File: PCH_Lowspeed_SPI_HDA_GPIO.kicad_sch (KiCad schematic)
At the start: 1 part

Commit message: Some DP and power work
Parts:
- added R1, R3: 30Ω, Resistor_SMD:R_0402_1005Metric, symbol Device:R_Small
- added R2: 20Ω, Resistor_SMD:R_0402_1005Metric, symbol Device:R_Small
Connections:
- net iGPU_DDI1_SCL: now reaches UPCH1.AL13 (GPP_I5/DDPB_CTRLCLK)
- net iGPU_DDI1_SDA: now reaches UPCH1.AR8 (GPP_I6/DDPB_CTRLDATA)
- net at UPCH1.AM2 (HDACPU_SDO): now also R1.2
- net at UPCH1.AM3 (HDACPU_SCLK): now also R3.2
- net at UPCH1.AN3 (HDACPU_SDI): now also R2.2
- new net CPU_DisplayAudio_CLK: R3.1
- new net CPU_DisplayAudio_SDI: R1.1
- new net CPU_DisplayAudio_SDO: R2.1

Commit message: More DP
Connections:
- net iGPU_DDI2_SDA: now reaches UPCH1.AL10 (GPP_I8/DDPC_CTRLDATA)
- net iGPU_DDI3_SCL: now reaches UPCH1.AL9 (GPP_I9/DDPD_CTRLCLK)
- net iGPU_DDI2_SCL: now reaches UPCH1.AN13 (GPP_I7/DDPC_CTRLCLK)
- net iGPU_DDI3_SDA: now reaches UPCH1.AR3 (GPP_I10/DDPD_CTRLDATA)
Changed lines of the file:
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@@
+	(wire
+		(pts
+			(xy 120.65 123.19) (xy 115.57 123.19)
+		)
+		(stroke
+			(width 0)
+			(type default)
+		)
+	)
 	(wire
 		(pts
@@
 	(wire
 		(pts
+			(xy 120.65 130.81) (xy 115.57 130.81)
+		)
+		(stroke
+			(width 0)
+			(type default)
+		)
+	)
+	(wire
+		(pts
+			(xy 120.65 128.27) (xy 115.57 128.27)
+		)
+		(stroke
+			(width 0)
+			(type default)
+		)
+	)
+	(wire
+		(pts
+			(xy 120.65 125.73) (xy 115.57 125.73)
+		)
+		(stroke
+			(width 0)
+			(type default)
+		)
+	)
+	(wire
+		(pts
 			(xy 158.75 57.15) (xy 162.56 57.15)
 		)
@@
 		)
 	)
+	(global_label "iGPU_DDI3_SDA"
+		(shape input)
+		(at 120.65 130.81 0)
+		(fields_autoplaced yes)
+		(effects
+			(font
+				(size 1.27 1.27)
+			)
+			(justify left)
+		)
+		(property "Intersheetrefs" "${INTERSHEET_REFS}"
+			(at 144.9831 130.81 0)
+			(effects
+				(font
+					(size 1.27 1.27)
+				)
+				(justify left)
+				(hide yes)
+			)
+		)
+	)
+	(global_label "iGPU_DDI2_SCL"
+		(shape input)
+		(at 120.65 123.19 0)
+		(fields_autoplaced yes)
+		(effects
+			(font
+				(size 1.27 1.27)
+			)
+			(justify left)
+		)
+		(property "Intersheetrefs" "${INTERSHEET_REFS}"
+			(at 144.9831 123.19 0)
+			(effects
+				(font
+					(size 1.27 1.27)
+				)
+				(justify left)
+				(hide yes)
+			)
+		)
+	)
 	(global_label "CPU_DisplayAudio_CLK"
 		(shape input)
@@
 		)
 	)
+	(global_label "iGPU_DDI3_SCL"
+		(shape input)
+		(at 120.65 128.27 0)
+		(fields_autoplaced yes)
+		(effects
+			(font
+				(size 1.27 1.27)
+			)
+			(justify left)
+		)
+		(property "Intersheetrefs" "${INTERSHEET_REFS}"
+			(at 144.9831 128.27 0)
+			(effects
+				(font
+					(size 1.27 1.27)
+				)
+				(justify left)
+				(hide yes)
+			)
+		)
+	)
 	(global_label "iGPU_DDI1_SCL"
 		(shape input)
@@
 			(effects
 				(font
+					(size 1.27 1.27)
+				)
+				(justify left)
+				(hide yes)
+			)
+		)
+	)
+	(global_label "iGPU_DDI2_SDA"
+		(shape input)
+		(at 120.65 125.73 0)
+		(fields_autoplaced yes)
+		(effects
+			(font
+				(size 1.27 1.27)
+			)
+			(justify left)
+		)
+		(property "Intersheetrefs" "${INTERSHEET_REFS}"
+			(at 144.9831 125.73 0)
+			(effects
+				(font

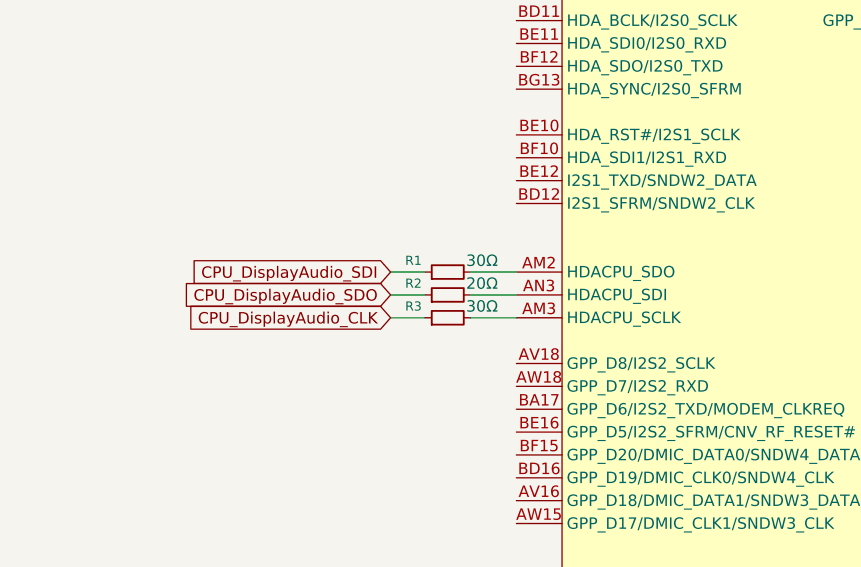
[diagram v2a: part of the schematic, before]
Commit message: Added PCH SKU IO table screenshot from datasheet to schematic
and a note about display audio
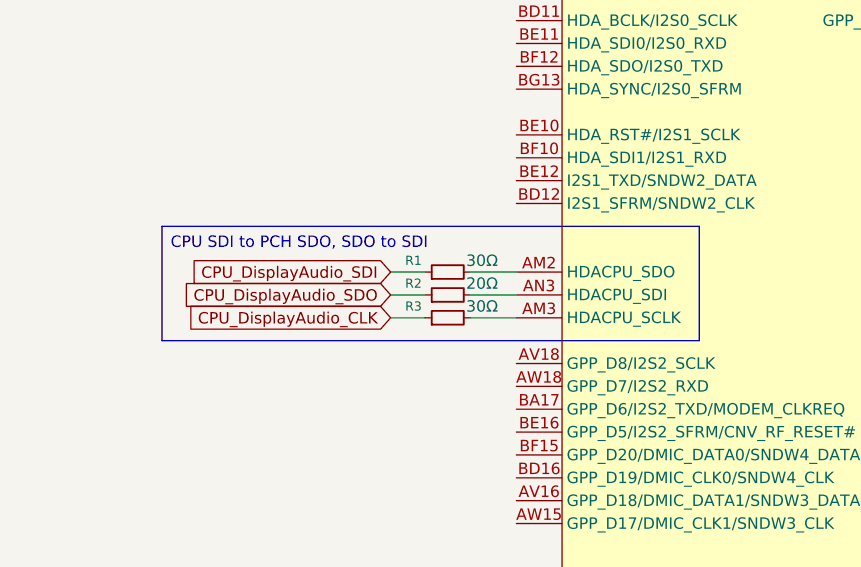
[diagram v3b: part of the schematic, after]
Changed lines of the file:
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@@
 		(company "WifiCable")
+	)
+	(text_box "CPU SDI to PCH SDO, SDO to SDI"
+		(exclude_from_sim no)
+		(at 133.35 52.07 0)
+		(size 59.69 12.7)
+		(margins 0.9525 0.9525 0.9525 0.9525)
+		(stroke
+			(width 0)
+			(type solid)
+		)
+		(fill
+			(type none)
+		)
+		(effects
+			(font
+				(size 1.27 1.27)
+			)
+			(justify left top)
+		)
 	)
 	(wire

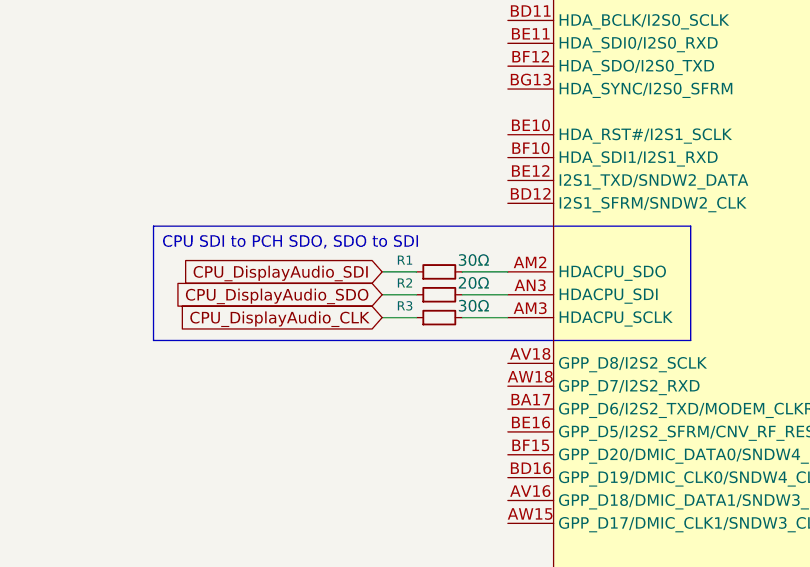
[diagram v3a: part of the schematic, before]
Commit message: partially added eDP + rearranged other display stuff
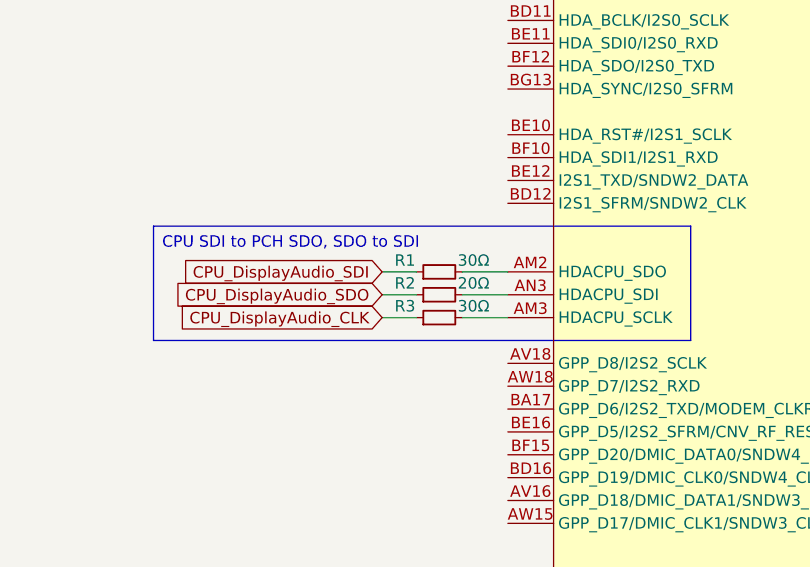
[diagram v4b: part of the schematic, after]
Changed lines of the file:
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@@
 			(effects
 				(font
-					(size 1.016 1.016)
+					(size 1.27 1.27)
 				)
 			)
@@
 			(effects
 				(font
-					(size 1.016 1.016)
+					(size 1.27 1.27)
 				)
 			)
@@
 			(effects
 				(font
-					(size 1.016 1.016)
+					(size 1.27 1.27)
 				)
 			)

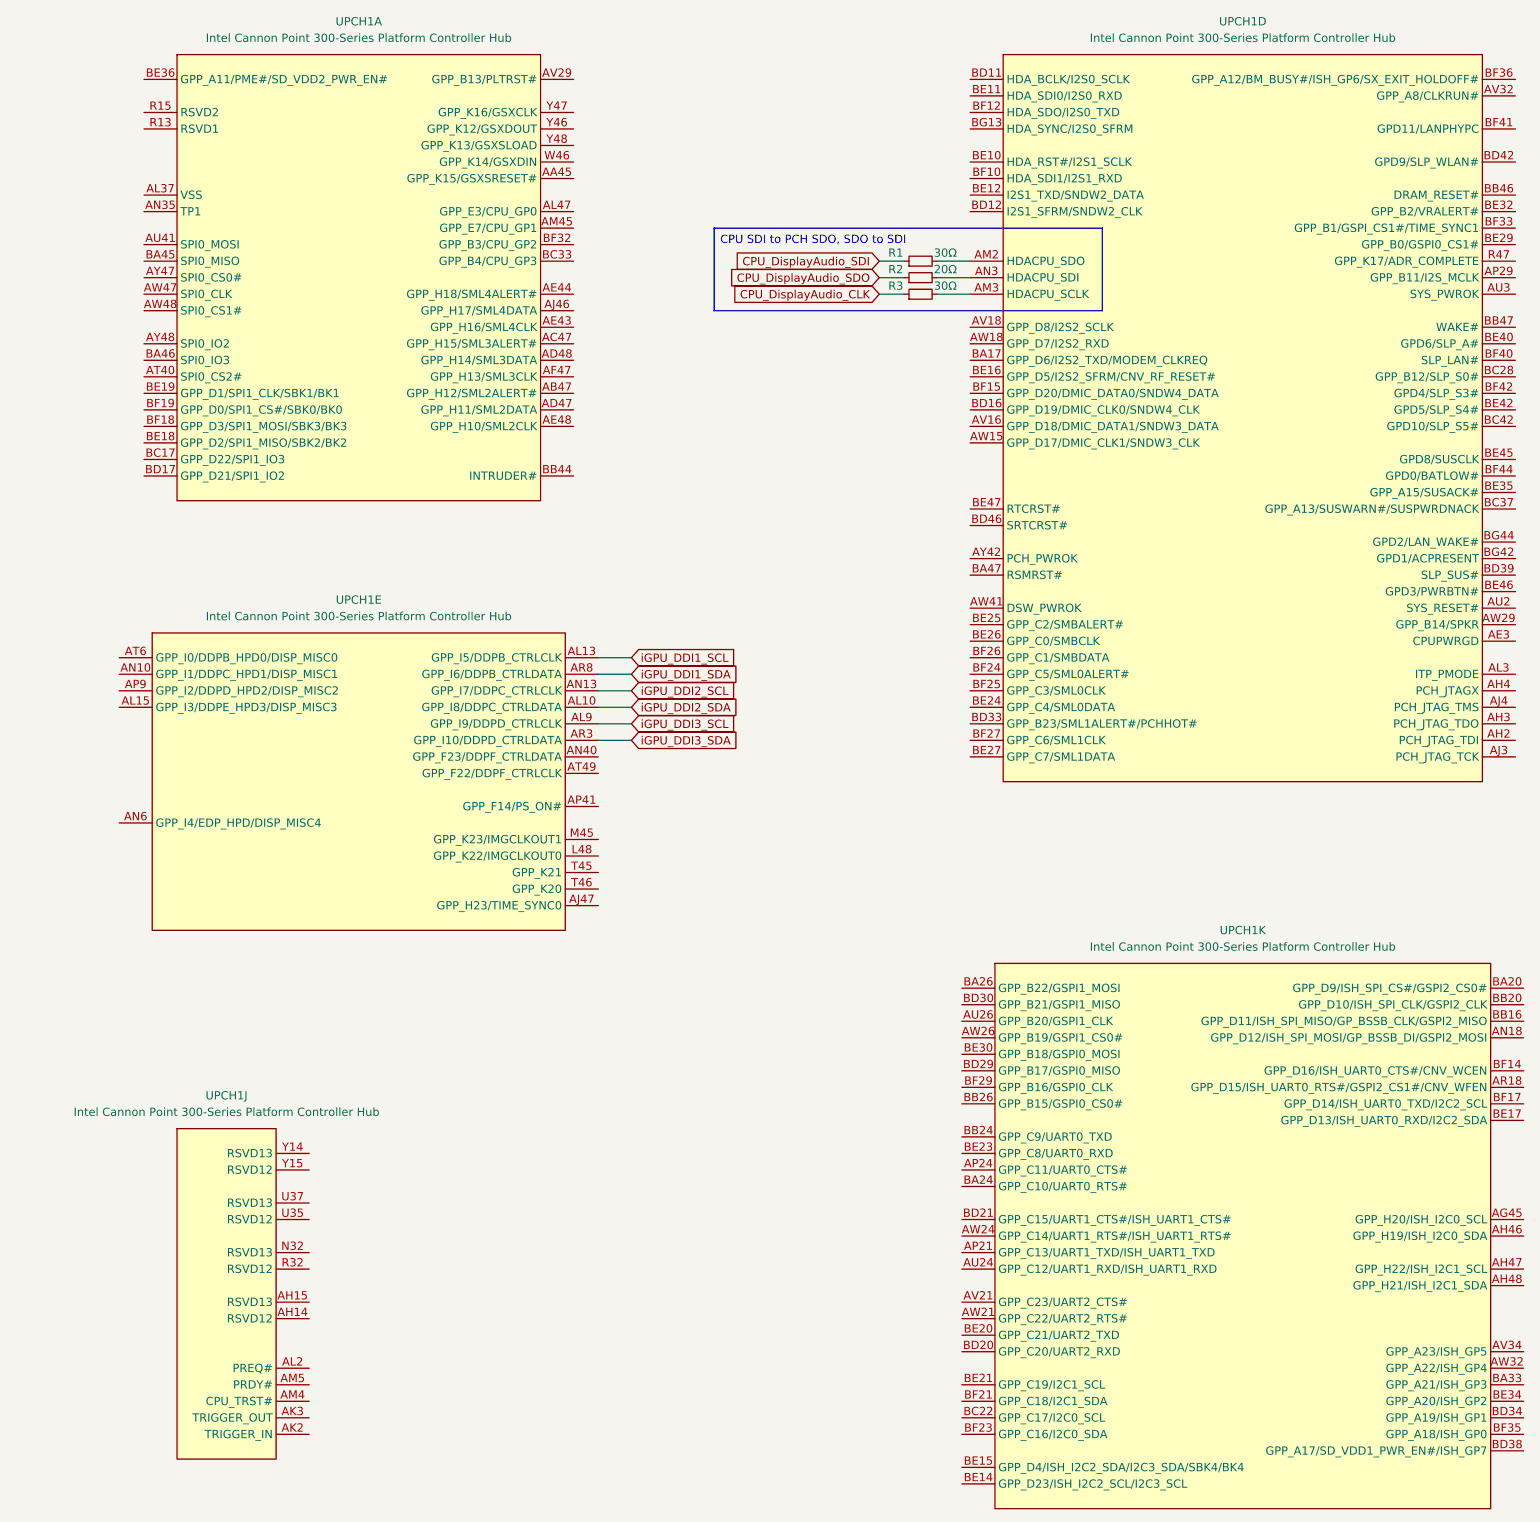
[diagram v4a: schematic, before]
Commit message: Added PCH PCIe rootport/bifurcation notes
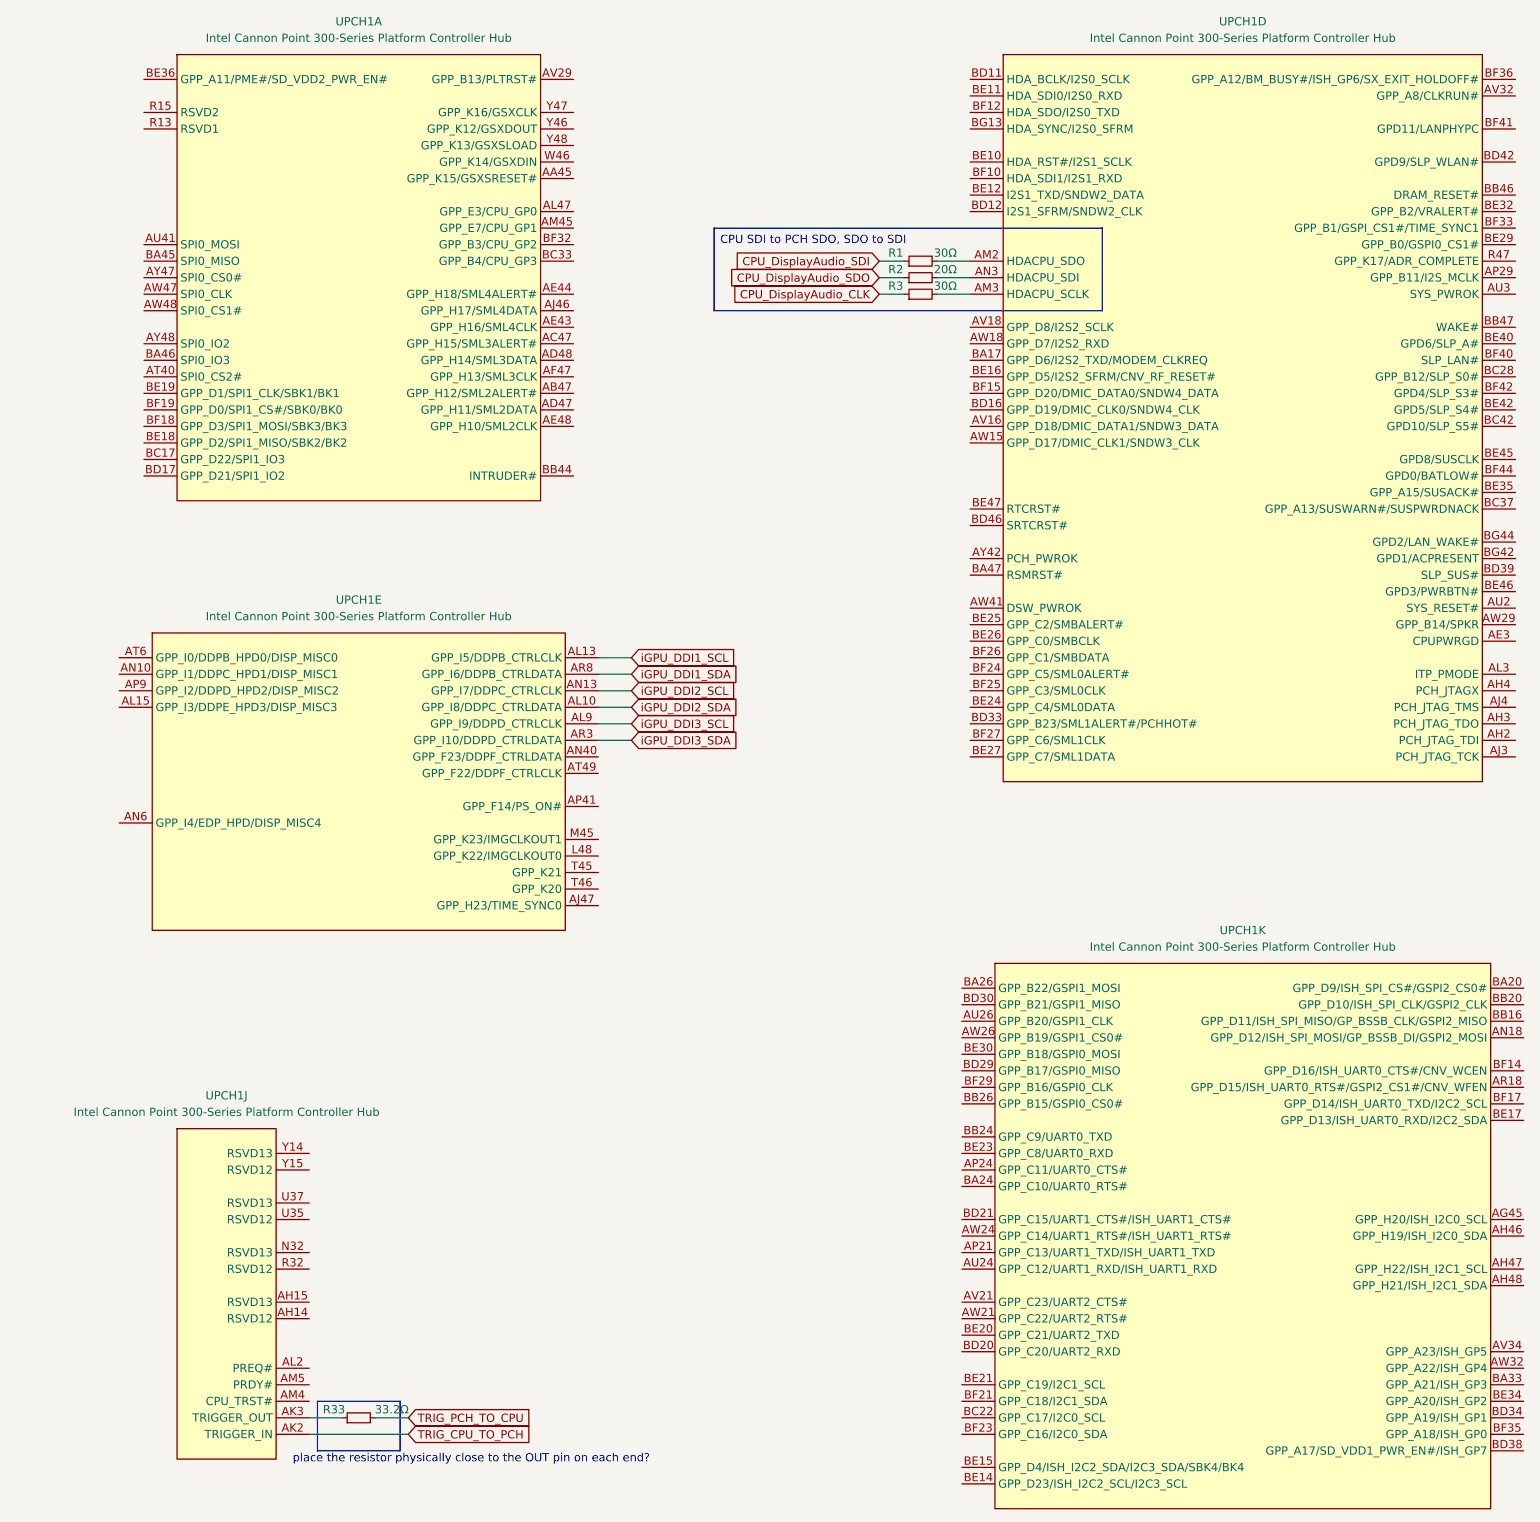
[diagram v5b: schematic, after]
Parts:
- added R33: 33.2Ω, Resistor_SMD:R_0402_1005Metric, symbol Device:R_Small
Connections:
- net TRIG_CPU_TO_PCH: now reaches UPCH1.AK2 (TRIGGER_IN)
- net at UPCH1.AK3 (TRIGGER_OUT): now also R33.1
- new net TRIG_PCH_TO_CPU: R33.2
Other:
- note added: "place the resistor physically close to the OUT pin on each end?"
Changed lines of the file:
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@@
 		(company "WifiCable")
 	)
+	(rectangle
+		(start 72.39 232.41)
+		(end 85.09 240.03)
+		(stroke
+			(width 0)
+			(type default)
+		)
+		(fill
+			(type none)
+		)
+	)
+	(text "place the resistor physically close to the OUT pin on each end?"
+		(exclude_from_sim no)
+		(at 68.58 241.3 0)
+		(effects
+			(font
+				(size 1.27 1.27)
+			)
+			(justify left)
+		)
+	)
 	(text_box "CPU SDI to PCH SDO, SDO to SDI"
 		(exclude_from_sim no)
@@
 	(wire
 		(pts
+			(xy 86.36 234.95) (xy 81.28 234.95)
+		)
+		(stroke
+			(width 0)
+			(type default)
+		)
+	)
+	(wire
+		(pts
 			(xy 120.65 120.65) (xy 115.57 120.65)
 		)
@@
 	(wire
 		(pts
+			(xy 71.12 237.49) (xy 86.36 237.49)
+		)
+		(stroke
+			(width 0)
+			(type default)
+		)
+	)
+	(wire
+		(pts
 			(xy 167.64 57.15) (xy 172.72 57.15)
 		)
@@
 	(wire
 		(pts
+			(xy 71.12 234.95) (xy 76.2 234.95)
+		)
+		(stroke
+			(width 0)
+			(type default)
+		)
+	)
+	(wire
+		(pts
 			(xy 120.65 125.73) (xy 115.57 125.73)
 		)
@@
 		)
 	)
+	(global_label "TRIG_PCH_TO_CPU"
+		(shape input)
+		(at 86.36 234.95 0)
+		(fields_autoplaced yes)
+		(effects
+			(font
+				(size 1.27 1.27)
+			)
+			(justify left)
+		)
+		(property "Intersheetrefs" "${INTERSHEET_REFS}"
+			(at 101.501 234.95 0)
+			(effects
+				(font
+					(size 1.27 1.27)
+				)
+				(justify left)
+				(hide yes)
+			)
+		)
+	)
 	(global_label "iGPU_DDI3_SDA"
 		(shape input)
@@
 		)
 	)
+	(global_label "TRIG_CPU_TO_PCH"
+		(shape input)
+		(at 86.36 237.49 0)
+		(fields_autoplaced yes)
+		(effects
+			(font
+				(size 1.27 1.27)
+			)
+			(justify left)
+		)
+		(property "Intersheetrefs" "${INTERSHEET_REFS}"
+			(at 101.501 237.49 0)
+			(effects
+				(font
+					(size 1.27 1.27)
+				)
+				(justify left)
+				(hide yes)
+			)
+		)
+	)
 	(global_label "CPU_DisplayAudio_CLK"
 		(shape input)
@@
 		)
 		(instances
-			(project "Stroopwafel-LGA1151-CFL"
+			(project ""
+				(path "/4bc771b8-eb19-46d0-8798-27231a7c6e83/55a4f655-ea62-4675-bc34-60bbcfd07a2f"
+					(reference "UPCH1")
+					(unit 10)
+				)
 				(path "/4bc771b8-eb19-46d0-8798-27231a7c6e83/cd978078-9495-426d-921d-88f146c11707"
 					(reference "UPCH1")
@@
 	)
 	(symbol
+		(lib_name "Intel_CFL_PCH_FCBGA874_but_better_2")
 		(lib_id "A-my-stuff:Intel_CFL_PCH_FCBGA874_but_better")
 		(at 78.74 139.7 0)
@@
 		)
 		(instances
-			(project "Stroopwafel-LGA1151-CFL"
+			(project ""
+				(path "/4bc771b8-eb19-46d0-8798-27231a7c6e83/55a4f655-ea62-4675-bc34-60bbcfd07a2f"
+					(reference "UPCH1")
+					(unit 5)
+				)
 				(path "/4bc771b8-eb19-46d0-8798-27231a7c6e83/cd978078-9495-426d-921d-88f146c11707"
 					(reference "UPCH1")
@@
 	)
 	(symbol
-		(lib_name "Intel_CFL_PCH_FCBGA874_but_better_1")
+		(lib_name "Intel_CFL_PCH_FCBGA874_but_better_4")
 		(lib_id "A-my-stuff:Intel_CFL_PCH_FCBGA874_but_better")
 		(at 78.74 50.8 0)
@@
 		(pin "G2"
 		)
-		(pin "AL37"
-		)
-		(pin "AN35"
-		)
 		(instances
-			(project "Stroopwafel-LGA1151-CFL"
+			(project ""
+				(path "/4bc771b8-eb19-46d0-8798-27231a7c6e83/55a4f655-ea62-4675-bc34-60bbcfd07a2f"
+					(reference "UPCH1")
+					(unit 1)
+				)
 				(path "/4bc771b8-eb19-46d0-8798-27231a7c6e83/cd978078-9495-426d-921d-88f146c11707"
 					(reference "UPCH1")
@@
 	)
 	(symbol
+		(lib_name "Intel_CFL_PCH_FCBGA874_but_better_1")
 		(lib_id "A-my-stuff:Intel_CFL_PCH_FCBGA874_but_better")
 		(at 214.63 190.5 0)
@@
 		)
 		(instances
-			(project "Stroopwafel-LGA1151-CFL"
+			(project ""
+				(path "/4bc771b8-eb19-46d0-8798-27231a7c6e83/55a4f655-ea62-4675-bc34-60bbcfd07a2f"
+					(reference "UPCH1")
+					(unit 11)
+				)
 				(path "/4bc771b8-eb19-46d0-8798-27231a7c6e83/cd978078-9495-426d-921d-88f146c11707"
 					(reference "UPCH1")
@@
 	)
 	(symbol
+		(lib_id "Device:R_Small")
+		(at 78.74 234.95 90)
+		(unit 1)
+		(exclude_from_sim no)
+		(in_bom yes)
+		(on_board yes)
+		(dnp no)
+		(property "Reference" "R33"
+			(at 74.93 233.68 90)
+			(effects
+				(font
+					(size 1.27 1.27)
+				)
+			)
+		)
+		(property "Value" "33.2Ω"
+			(at 83.82 233.68 90)
+			(effects
+				(font
+					(size 1.27 1.27)
+				)
+			)
+		)
+		(property "Footprint" "Resistor_SMD:R_0402_1005Metric"
+			(at 78.74 234.95 0)
+			(effects
+				(font
+					(size 1.27 1.27)
+				)
+				(hide yes)
+			)
+		)
+		(property "Datasheet" "~"
+			(at 78.74 234.95 0)
+			(effects
+				(font
+					(size 1.27 1.27)
+				)
+				(hide yes)
+			)
+		)
+		(property "Description" "Resistor, small symbol"
+			(at 78.74 234.95 0)
+			(effects
+				(font
+					(size 1.27 1.27)
+				)
+				(hide yes)
+			)
+		)
+		(pin "2"
+		)
+		(pin "1"
+		)
+		(instances
+			(project "Stroopwafel-LGA1151-CFL"
+				(path "/4bc771b8-eb19-46d0-8798-27231a7c6e83/cd978078-9495-426d-921d-88f146c11707"
+					(reference "R33")
+					(unit 1)
+				)
+			)
+		)
+	)
+	(symbol
+		(lib_name "Intel_CFL_PCH_FCBGA874_but_better_3")
 		(lib_id "A-my-stuff:Intel_CFL_PCH_FCBGA874_but_better")
 		(at 214.63 50.8 0)
@@
 		)
 		(instances
-			(project "Stroopwafel-LGA1151-CFL"
+			(project ""
+				(path "/4bc771b8-eb19-46d0-8798-27231a7c6e83/55a4f655-ea62-4675-bc34-60bbcfd07a2f"
+					(reference "UPCH1")
+					(unit 4)
+				)
 				(path "/4bc771b8-eb19-46d0-8798-27231a7c6e83/cd978078-9495-426d-921d-88f146c11707"
 					(reference "UPCH1")
